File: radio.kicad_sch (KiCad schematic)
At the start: 41 parts, among them J301 434MHz ANT pads, U301 CC1200, X301 40MHz

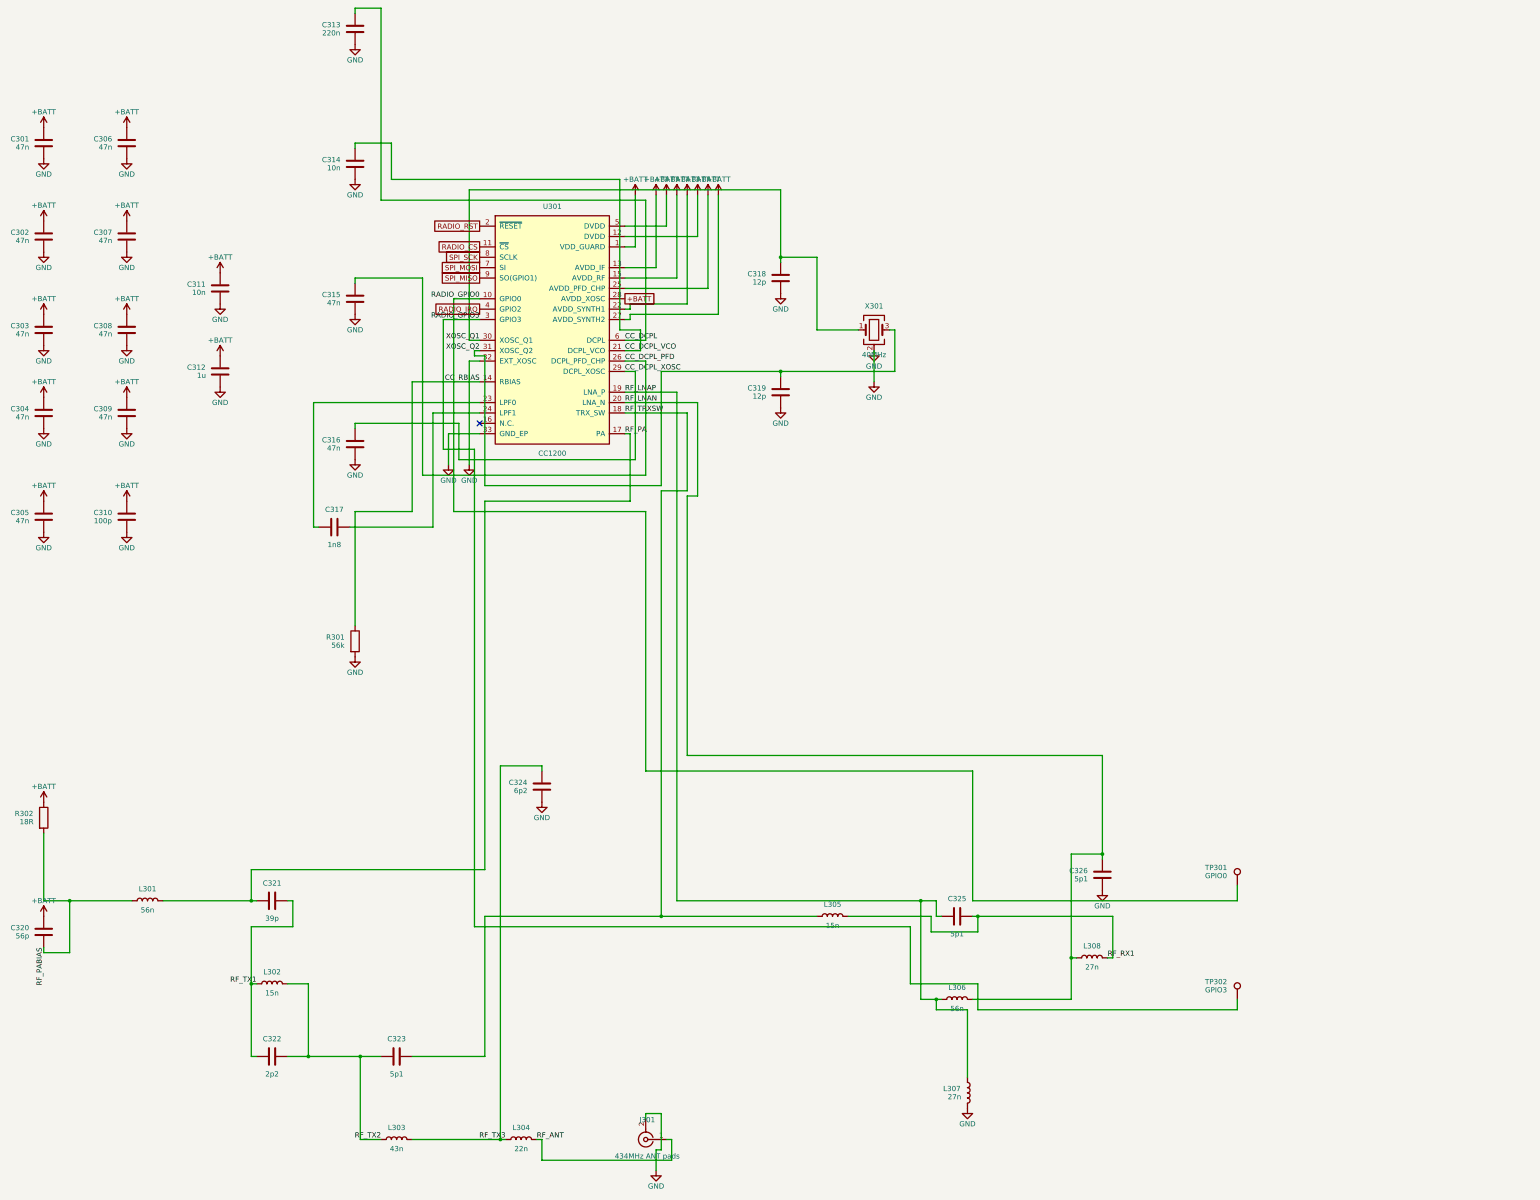
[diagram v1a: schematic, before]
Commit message: Clean up schematic. Add component groups to PCB.
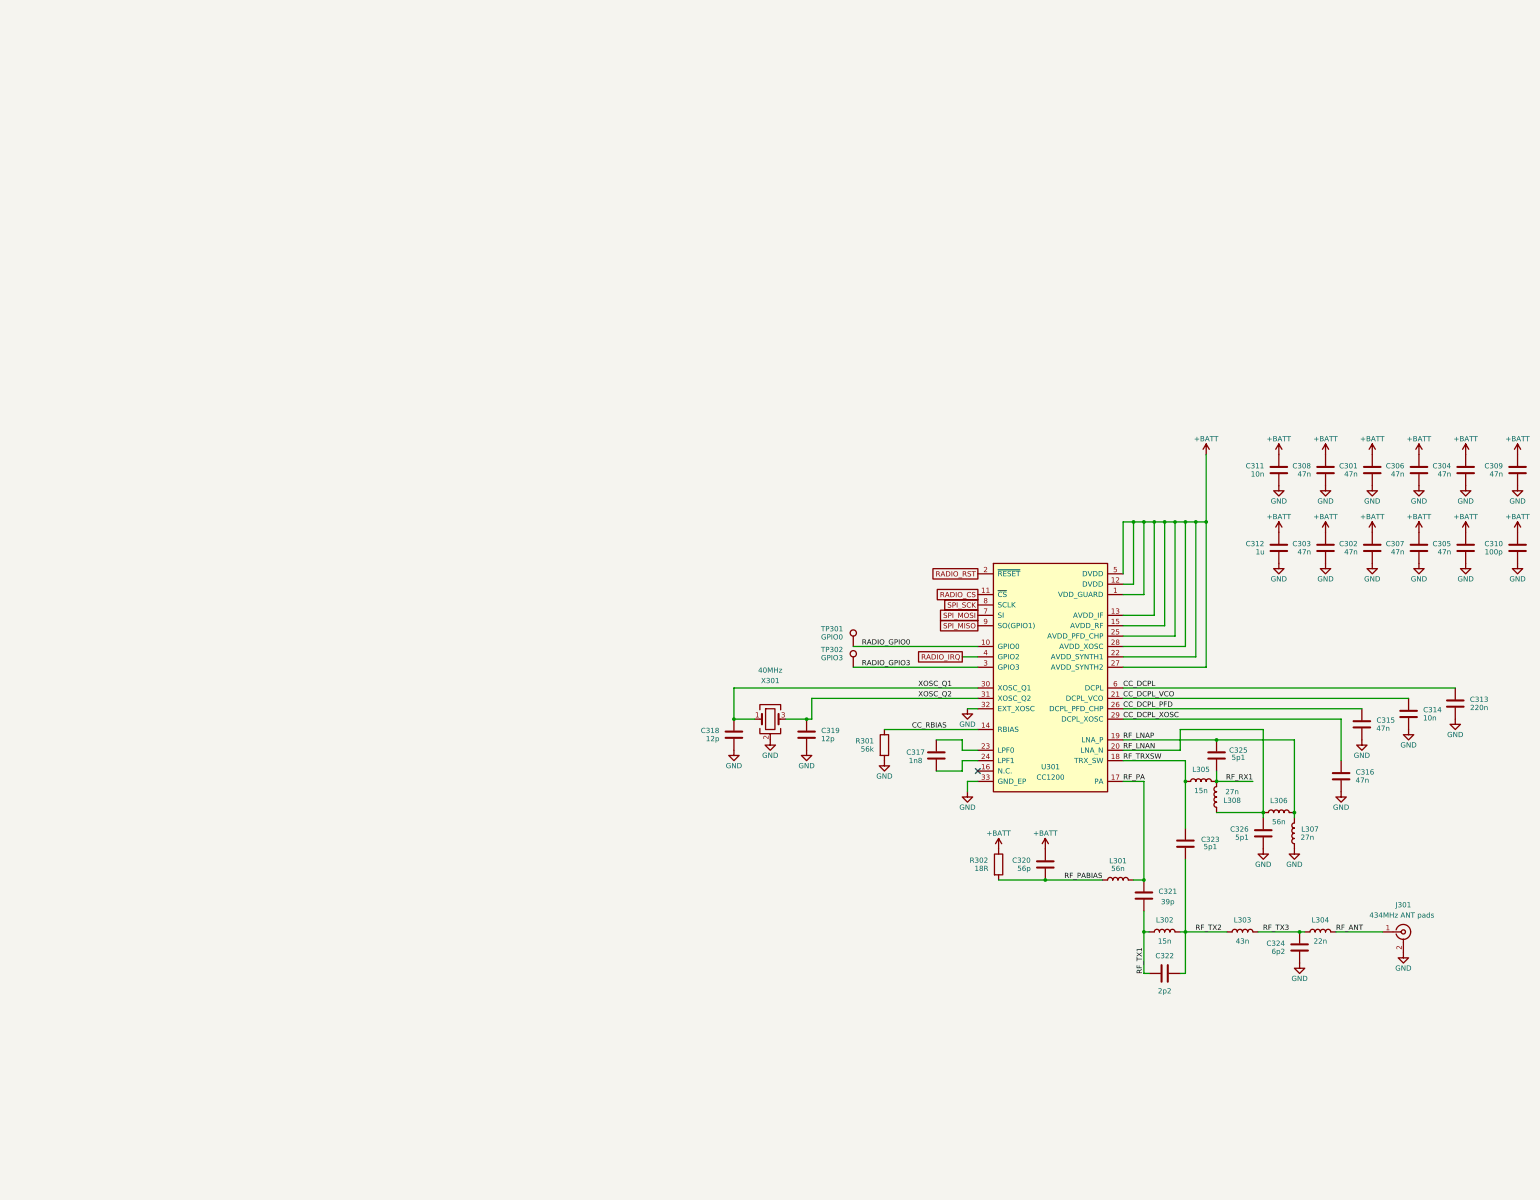
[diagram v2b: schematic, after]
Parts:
- J301: footprint cc1200_balloon:SolderPad_Coax_Pigtail -> Connector_Coaxial:SMA_Samtec_SMA-J-P-H-ST-EM1_EdgeMount
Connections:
- net RF_LNAP: now also C325.2; no longer C325.1
- net RF_PA: now also C321.2; no longer C321.1
- net RF_RX1: now also C325.1; no longer C325.2
- net RF_TX1: now also C321.1; no longer C321.2
- net at C317.1: now also U301.24 (LPF1); no longer U301.23 (LPF0)
- net at C317.2: now also U301.23 (LPF0); no longer U301.24 (LPF1)
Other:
- moved on the sheet: C301, C302, C303, C304, C305, C306, C307, C308, C309, C310, C311, C312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

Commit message: Inital routing
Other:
- moved on the sheet: C301, C302, C303, C304, C305, C306, C307, C308, C309, C310, C311, C312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

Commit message: Small adjustments.
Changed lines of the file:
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@@
 		(dnp no)
 		(property "Reference" "U301"
-			(at 284.48 221.234 0)
+			(at 284.48 165.862 0)
 			(show_name no)
 			(do_not_autoplace no)
@@
 		)
 		(property "Value" "CC1200"
-			(at 284.48 223.774 0)
+			(at 284.48 168.402 0)
 			(show_name no)
 			(do_not_autoplace no)
